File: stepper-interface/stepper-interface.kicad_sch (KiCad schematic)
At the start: 0 parts

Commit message: steppeer-controller -> stepper-interface
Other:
- title: stepper-controller -> stepper-interface
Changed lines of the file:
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@@
   (paper "A4")
   (title_block
-    (title "stepper-controller")
+    (title "stepper-interface")
     (date "2024-04-17")
     (rev "1.0")
@@
     )
     (instances
-      (project "stepper-controller"
+      (project "stepper-interface"
         (path "/df2b2e89-e055-4140-95de-f1df723db034" (page "4"))
       )
@@
     )
     (instances
-      (project "stepper-controller"
+      (project "stepper-interface"
         (path "/df2b2e89-e055-4140-95de-f1df723db034" (page "2"))
       )
@@
     )
     (instances
-      (project "stepper-controller"
+      (project "stepper-interface"
         (path "/df2b2e89-e055-4140-95de-f1df723db034" (page "13"))
       )
@@
     )
     (instances
-      (project "stepper-controller"
+      (project "stepper-interface"
         (path "/df2b2e89-e055-4140-95de-f1df723db034" (page "3"))
       )

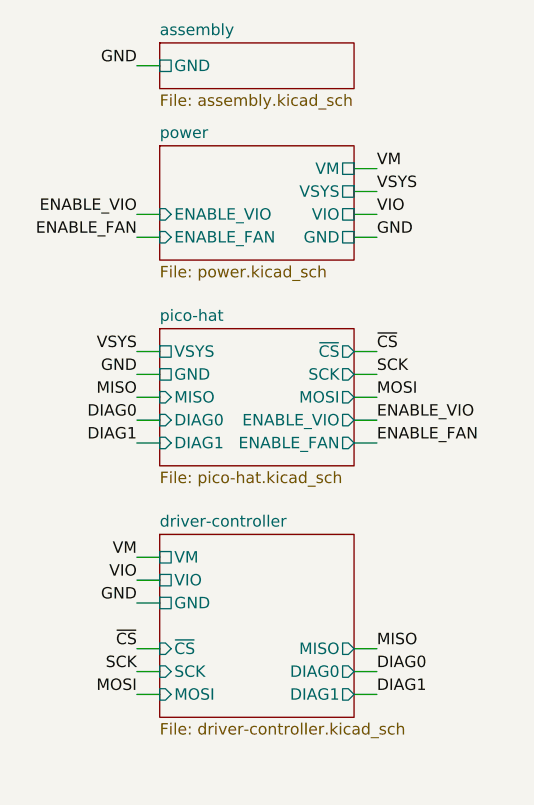
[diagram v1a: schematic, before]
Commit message: pico-hat -> microcontroller
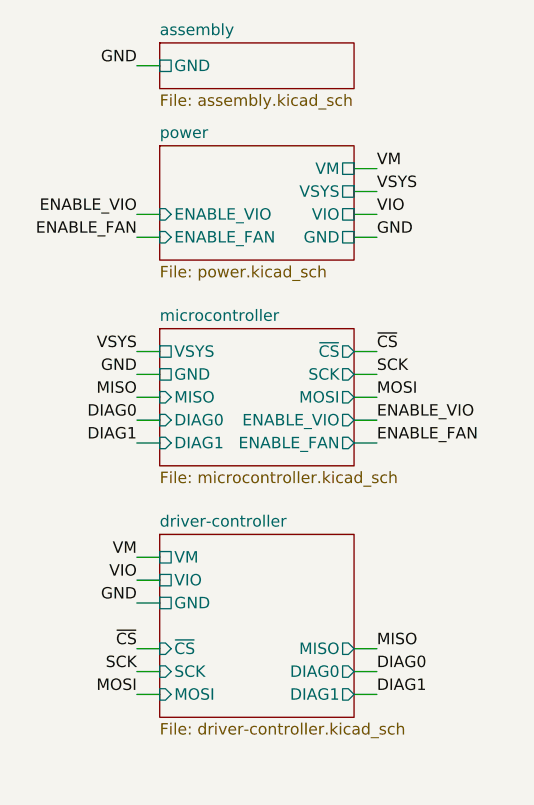
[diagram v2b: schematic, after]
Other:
- sheet pico-hat renamed microcontroller
- sheet microcontroller: file pico-hat.kicad_sch -> microcontroller.kicad_sch
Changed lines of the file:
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@@
   (title_block
     (title "stepper-interface")
-    (date "2024-04-17")
+    (date "2024-04-18")
     (rev "1.0")
     (company "Howard Hughes Medical Institute")
@@
     (stroke (width 0.1524) (type solid))
     (fill (color 0 0 0 0.0000))
-    (property "Sheetname" "pico-hat" (at 130.81 84.3784 0)
+    (property "Sheetname" "microcontroller" (at 130.81 84.3784 0)
       (effects (font (size 1.27 1.27)) (justify left bottom))
     )
-    (property "Sheetfile" "pico-hat.kicad_sch" (at 130.81 100.9146 0)
+    (property "Sheetfile" "microcontroller.kicad_sch" (at 130.81 100.9146 0)
       (effects (font (size 1.27 1.27)) (justify left top))
     )

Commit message: driver-controller -> controller-driver
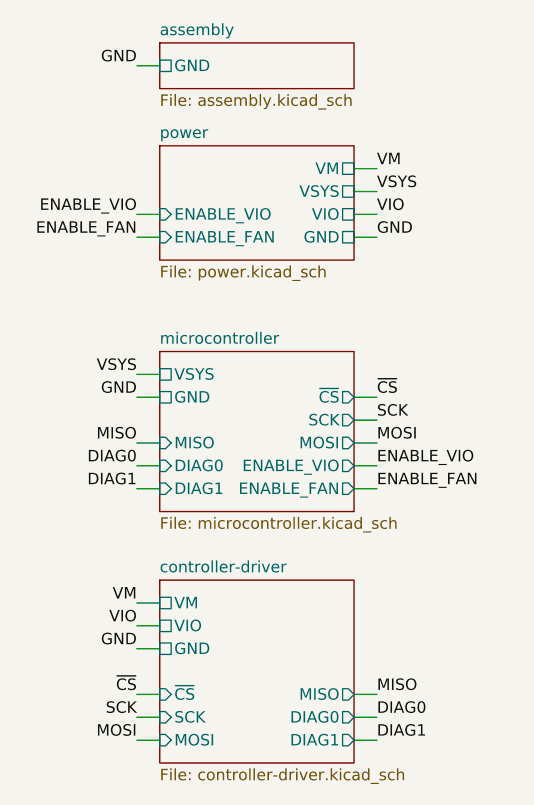
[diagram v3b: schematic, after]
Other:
- sheet driver-controller renamed controller-driver
- sheet controller-driver: file driver-controller.kicad_sch -> controller-driver.kicad_sch

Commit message: Add  microcontroller components
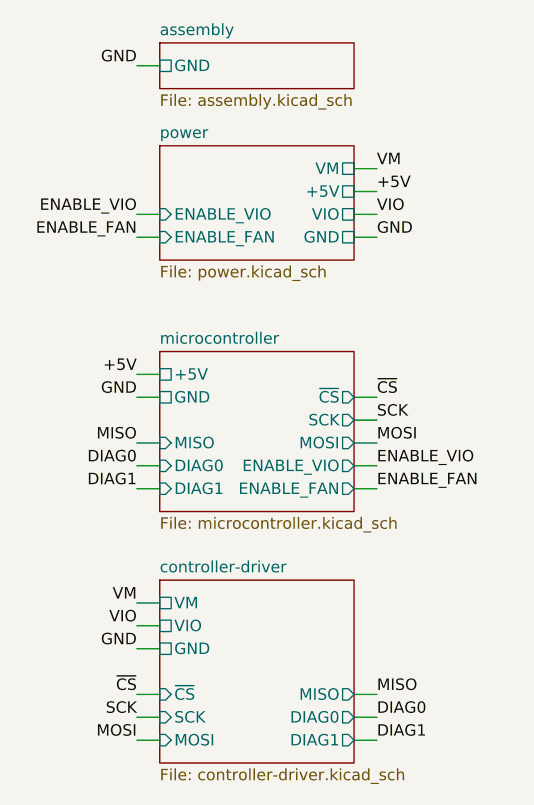
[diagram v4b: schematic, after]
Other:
- sheet microcontroller ports: added +5V; removed VSYS
- sheet power ports: added +5V; removed VSYS
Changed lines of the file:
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@@
   (title_block
     (title "stepper-interface")
-    (date "2024-04-18")
+    (date "2024-04-22")
     (rev "1.0")
     (company "Howard Hughes Medical Institute")
@@
     (effects (font (size 1.27 1.27)) (justify right bottom))
   )
-  (label "VSYS" (at 154.94 69.85 0) (fields_autoplaced)
+  (label "+5V" (at 154.94 69.85 0) (fields_autoplaced)
     (effects (font (size 1.27 1.27)) (justify left bottom))
   )
@@
     (effects (font (size 1.27 1.27)) (justify left bottom))
   )
-  (label "VSYS" (at 128.27 90.17 180) (fields_autoplaced)
+  (label "+5V" (at 128.27 90.17 180) (fields_autoplaced)
     (effects (font (size 1.27 1.27)) (justify right bottom))
   )
@@
       (effects (font (size 1.27 1.27)) (justify right))
     )
-    (pin "VSYS" passive (at 130.81 90.17 180)
+    (pin "+5V" passive (at 130.81 90.17 180)
       (effects (font (size 1.27 1.27)) (justify left))
     )
@@
       (effects (font (size 1.27 1.27)) (justify left))
     )
-    (pin "VSYS" passive (at 152.4 69.85 0)
-      (effects (font (size 1.27 1.27)) (justify right))
-    )
+    (pin "+5V" passive (at 152.4 69.85 0)
+      (effects (font (size 1.27 1.27)) (justify right))
+    )

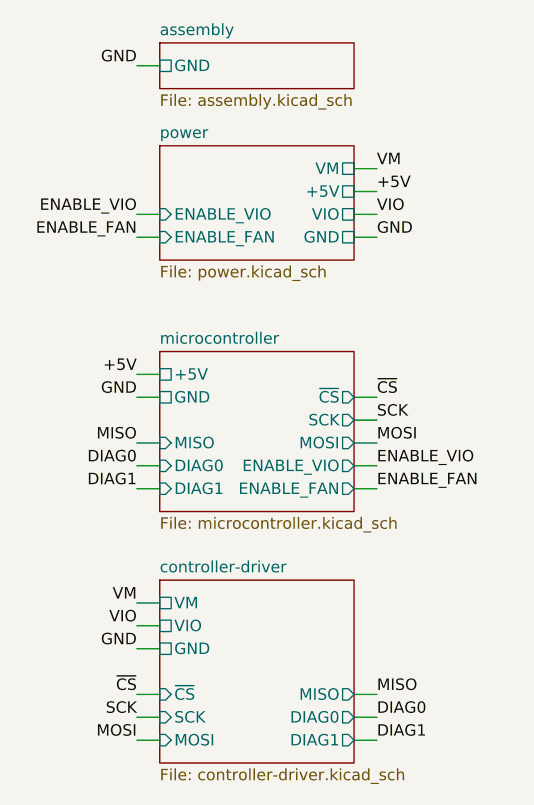
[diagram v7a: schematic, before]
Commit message: More specific sheet names
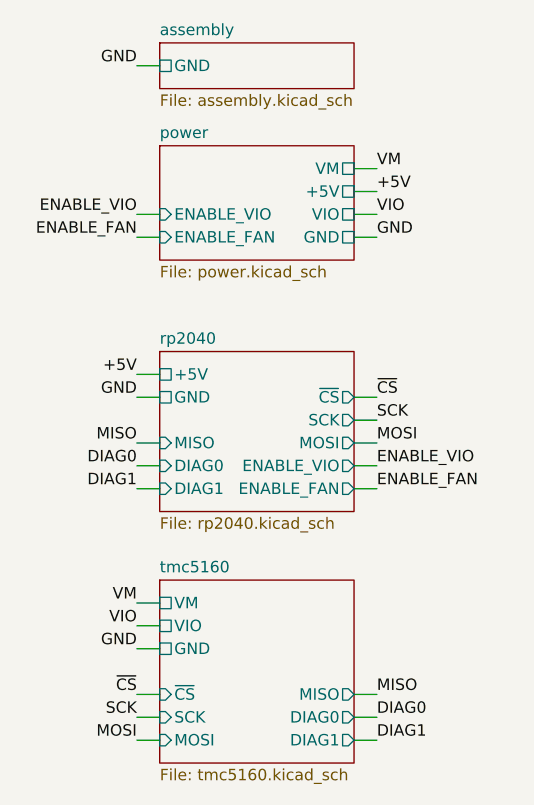
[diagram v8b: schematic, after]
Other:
- sheet controller-driver renamed tmc5160
- sheet microcontroller renamed rp2040
- sheet rp2040: file microcontroller.kicad_sch -> rp2040.kicad_sch
- sheet tmc5160: file controller-driver.kicad_sch -> tmc5160.kicad_sch
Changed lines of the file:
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@@
     (stroke (width 0.1524) (type solid))
     (fill (color 0 0 0 0.0000))
-    (property "Sheetname" "controller-driver" (at 130.81 112.3184 0)
+    (property "Sheetname" "tmc5160" (at 130.81 112.3184 0)
       (effects (font (size 1.27 1.27)) (justify left bottom))
     )
-    (property "Sheetfile" "controller-driver.kicad_sch" (at 130.81 133.9346 0)
+    (property "Sheetfile" "tmc5160.kicad_sch" (at 130.81 133.9346 0)
       (effects (font (size 1.27 1.27)) (justify left top))
     )
@@
     (stroke (width 0.1524) (type solid))
     (fill (color 0 0 0 0.0000))
-    (property "Sheetname" "microcontroller" (at 130.81 86.9184 0)
+    (property "Sheetname" "rp2040" (at 130.81 86.9184 0)
       (effects (font (size 1.27 1.27)) (justify left bottom))
     )
-    (property "Sheetfile" "microcontroller.kicad_sch" (at 130.81 105.9946 0)
+    (property "Sheetfile" "rp2040.kicad_sch" (at 130.81 105.9946 0)
       (effects (font (size 1.27 1.27)) (justify left top))
     )
